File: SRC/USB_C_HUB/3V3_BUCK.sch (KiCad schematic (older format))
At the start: 34 parts

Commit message: commit with all DFPs properly connected
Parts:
- added C? (x2): 10uF, symbol Device:C_Small
- added IC?: LP38501ATJ-ADJ_NOPB, LP38511TJADJNOPB, symbol SamacSys_Parts:LP38501ATJ-ADJ_NOPB
- added R? (x2): 10K, symbol Device:R_US
- added R?: 8.25K, symbol Device:R_US
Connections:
- net labels added: +1V1
- wire segments 133 -> 153
- no-connect marks 1 -> 2
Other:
- note added: "1.1V LDO"
- note added: "3.3V 5A BUCK CONVERTER"
- note added: "BOOST CONVERTER 5A 5V\n"
- moved on the sheet: C?, D?, L?, Q?, R?, U?

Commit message: all but HDMI + 2 DFP ports
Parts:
- removed C? (x2): 10uF, symbol Device:C_Small
- removed IC?: LP38501ATJ-ADJ_NOPB, LP38511TJADJNOPB, symbol SamacSys_Parts:LP38501ATJ-ADJ_NOPB
- removed R? (x2): 10K, symbol Device:R_US
- removed R?: 8.25K, symbol Device:R_US
- added C?: 10uF_1mOHM_402, symbol Device:C_Small
- added C?: 4.7uF, symbol Device:C_Small
- added C?: 120Pf_1mOHM, symbol Device:C_Small
- added C?: 1uF, symbol Device:C_Small
- added IC?: TPS62824ADMQR, TPS62824ADMQR, symbol SamacSys_Parts:TPS62824ADMQR
- added L?: 470nH_30m, symbol OLIMEX_RCL:INDUCTOR_SMALL
- added R?: 82.5K, symbol Device:R_US
- added R? (x2): 100K, symbol Device:R_US
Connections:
- wire segments 153 -> 165
- no-connect marks 2 -> 1
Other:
- note added: "1.1V BUCK CONVERTER\nHIGHLY EFFICIENT\n"
- note removed: "1.1V LDO"

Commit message: ALL DONE BUT THE HDMI SECTION. NEED FOOTPRINT ASSIGNMENT
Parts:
- IC5: renamed from IC?; footprint TPS62824ADMQR -> SamacSys_Parts_2:TPS62824ADMQR
- gave numbers to parts that had none: 41
- renumbered Ron to Ron1
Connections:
- net VBUS renamed SYS_PWR

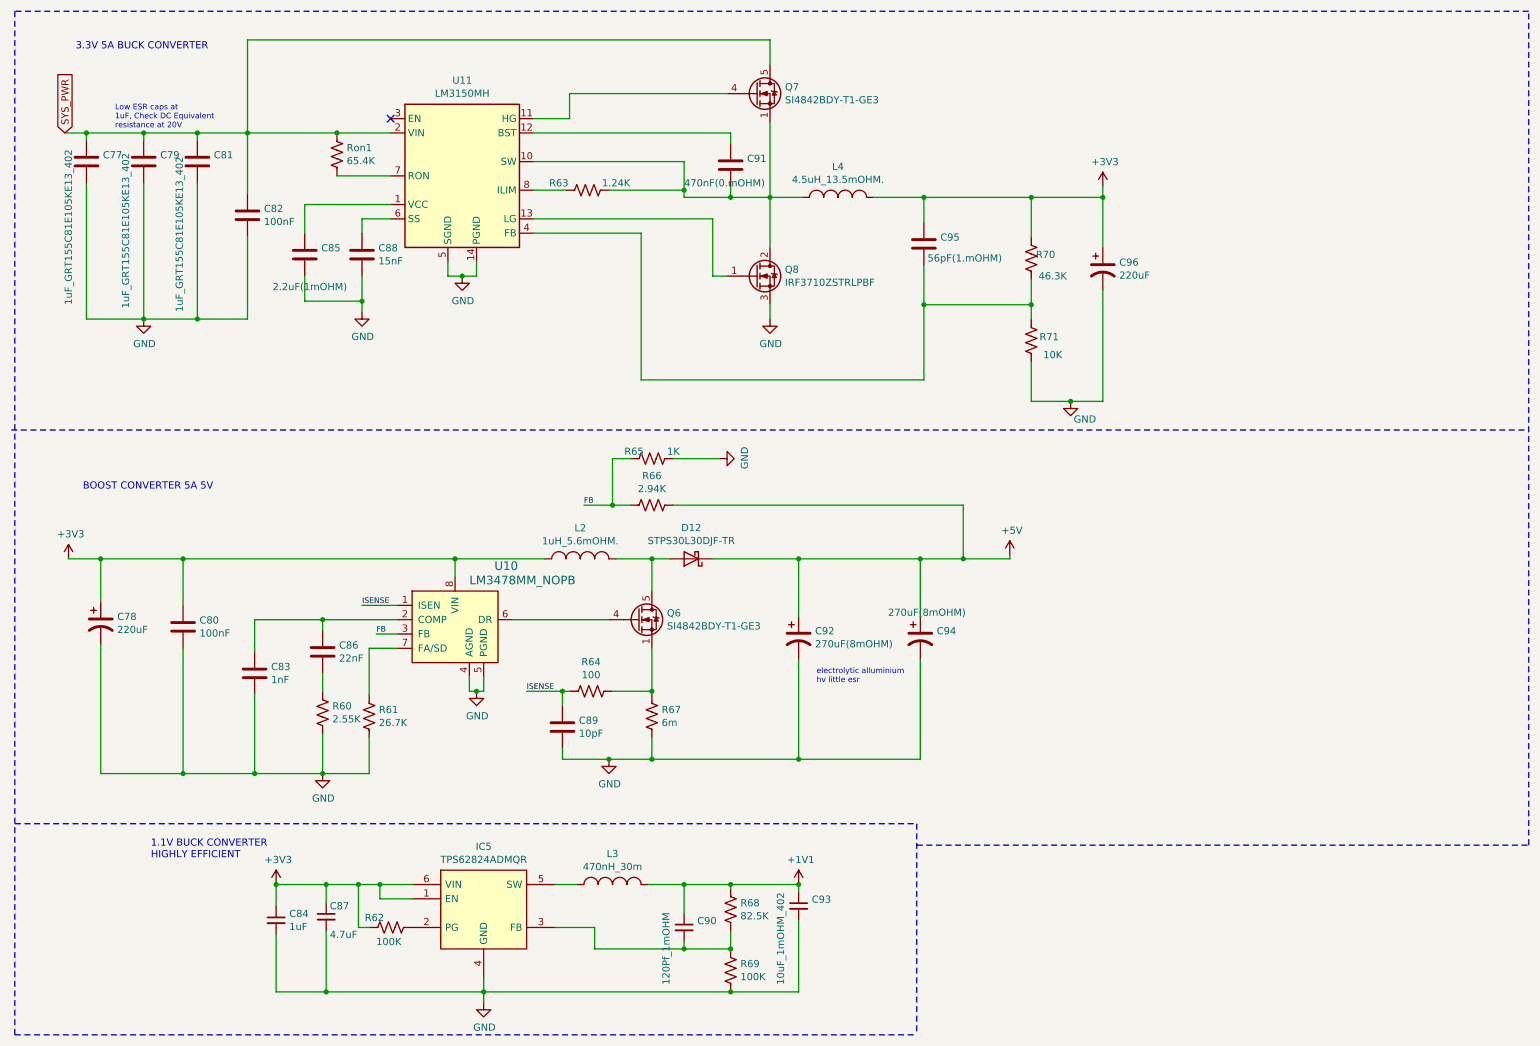
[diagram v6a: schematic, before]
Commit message: schematic capture complete. Pending Footprint assignment. accetable Errors=21
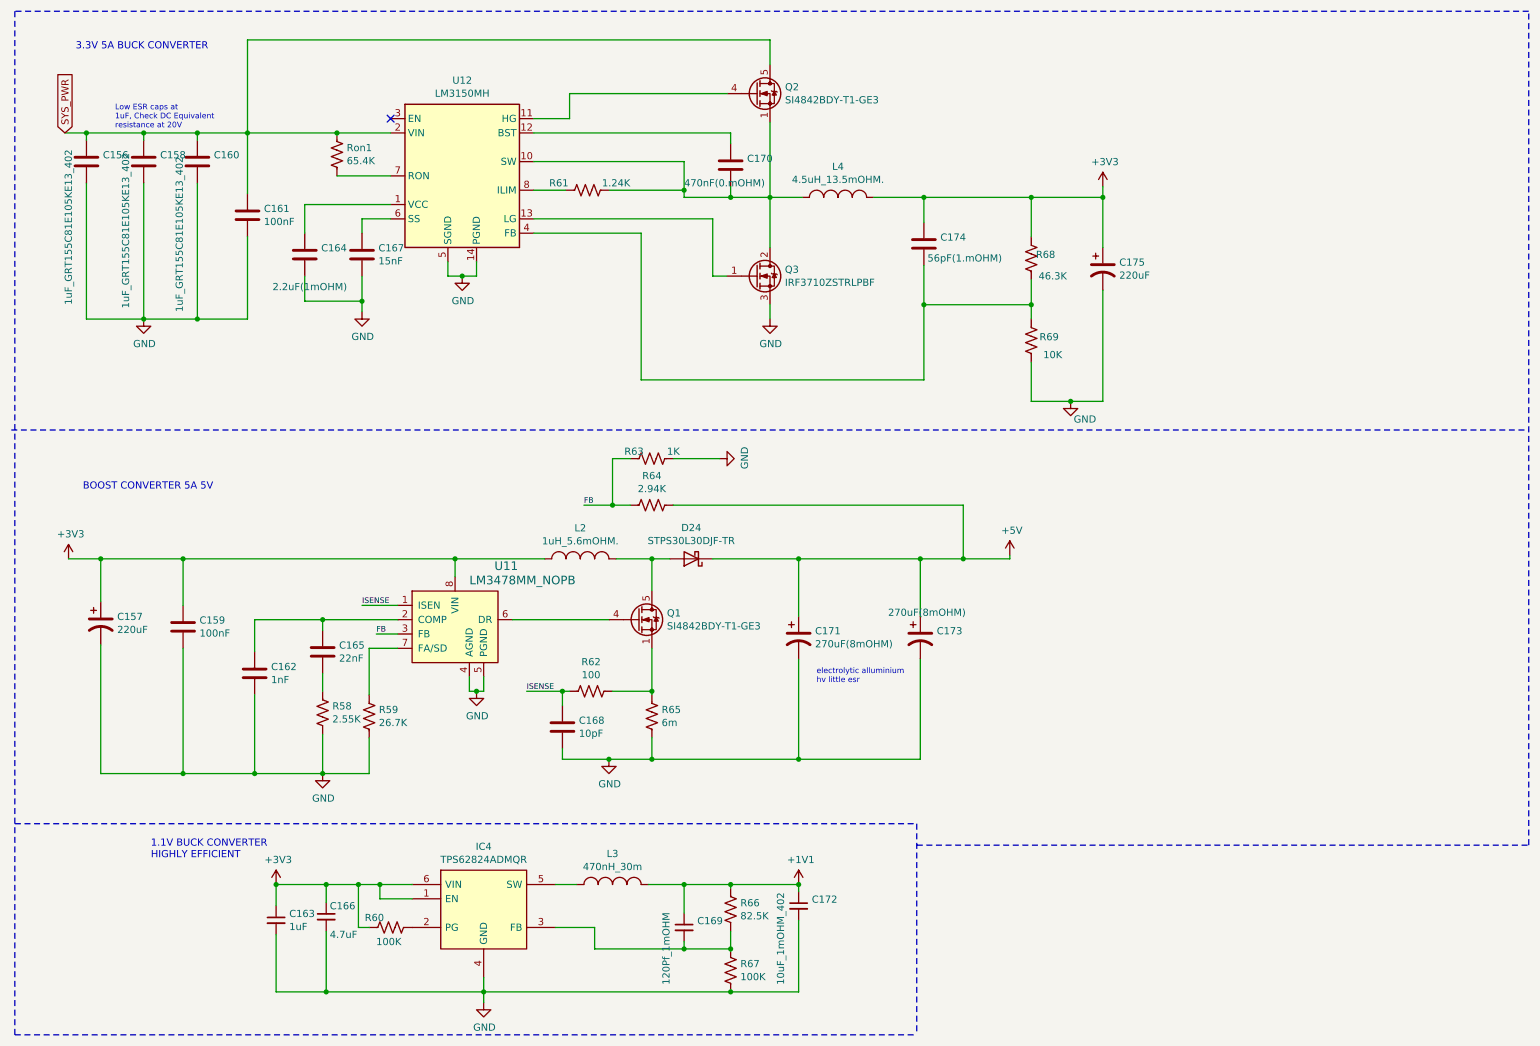
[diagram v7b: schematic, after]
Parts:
- renumbered C77 to C156, C78 to C157, C79 to C158, C80 to C159, C81 to C160, C82 to C161, C83 to C162, C84 to C163, C85 to C164, C86 to C165, C87 to C166, C88 to C167, C89 to C168, C90 to C169, C91 to C170, C92 to C171, C93 to C172, C94 to C173, C95 to C174, C96 to C175, D12 to D24, IC5 to IC4, Q6 to Q1, Q7 to Q2, Q8 to Q3, R60 to R58, R61 to R59, R62 to R60, R63 to R61, R64 to R62, R65 to R63, R66 to R64, R67 to R65, R68 to R66, R69 to R67, R70 to R68, R71 to R69, U10 to U11, U11 to U12
